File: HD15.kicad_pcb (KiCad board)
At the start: 2 copper layers, 110 x 62 mm, 46 parts, among them CN1 9, CN2 9, CN3 35RAPC4BH3, CN5 B6B-XH-A(LF)(SN), CN6 353180620, J1A JAMMA PINS 3.96MM PITCH 2.2MM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, J1B JAMMA PINS 3.96MM PITCH 2.2MM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, SW1 MJTP1230, SW2 MJTP1230, SW3 DIPSwitch-4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

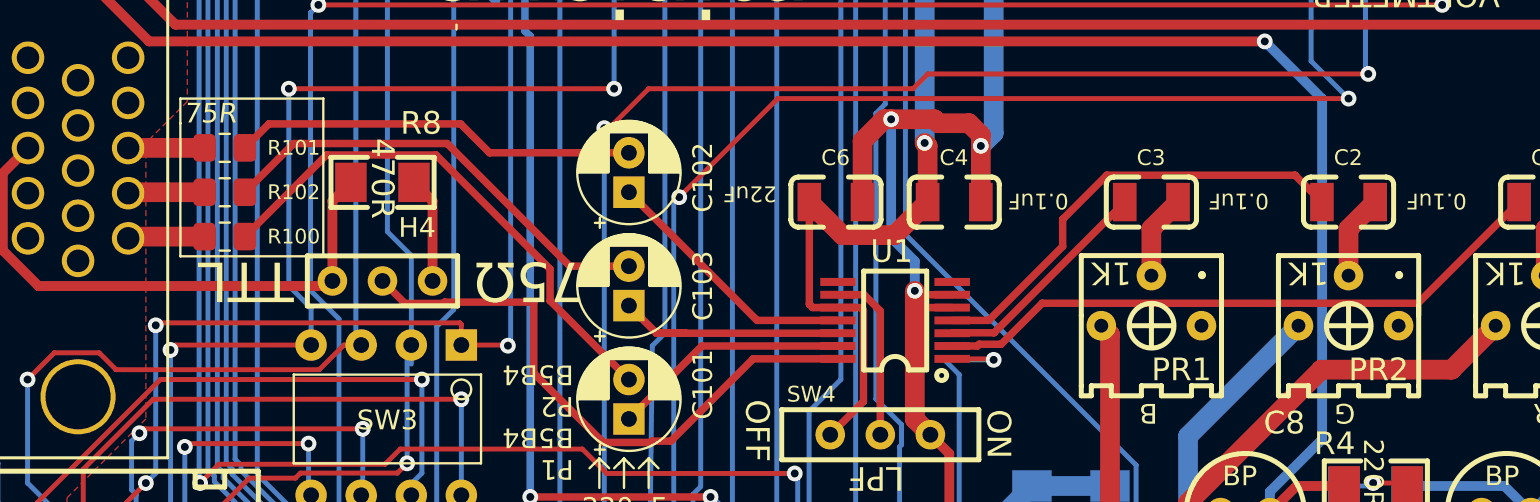
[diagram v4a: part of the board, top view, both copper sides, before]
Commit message: Fix RBG -> RGB screwup
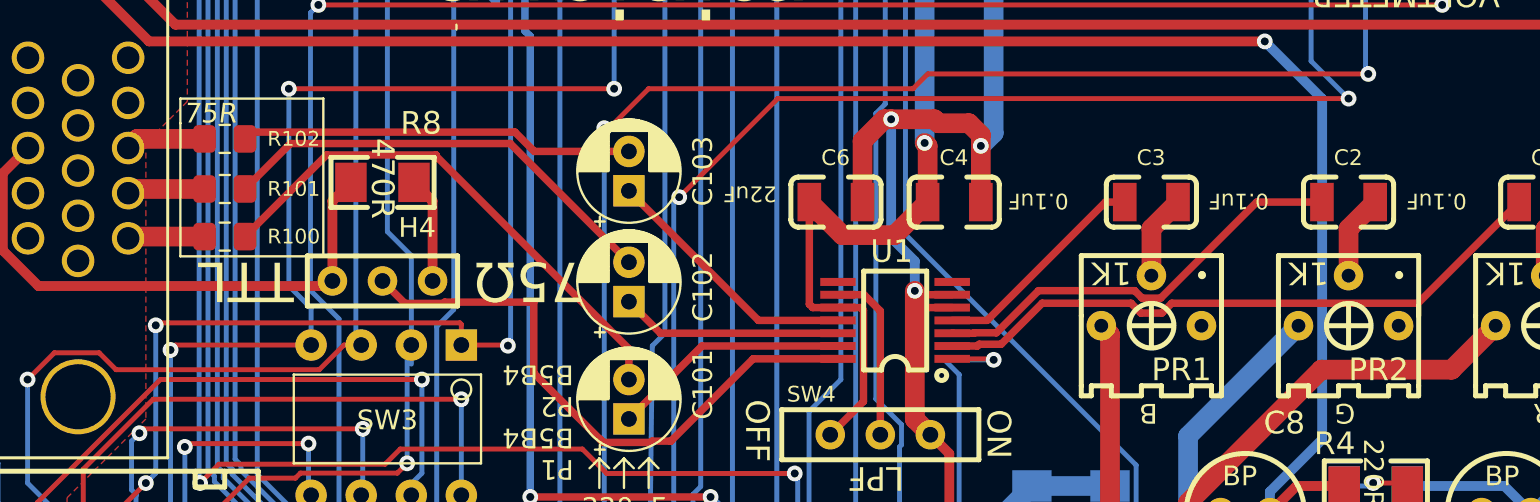
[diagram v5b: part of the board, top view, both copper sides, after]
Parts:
- moved C103 5.82 mm to (36.5, 13.4)
- moved C102 5.55 mm to (36.5, 19.1)
- moved R102 2.71 mm to (16.0, 10.8)
- moved R101 2.09 mm to (16.0, 13.3)
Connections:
- REF** pad 2: VIDEO_BLUE_5 -> VIDEO_GREEN_5
- REF** pad 3: VIDEO_GREEN_5 -> VIDEO_BLUE_5
- U1 pad 11: VIDEO_GREEN_3 -> VIDEO_BLUE_3
- U1 pad 12: VIDEO_BLUE_3 -> VIDEO_GREEN_3
- U1 pad 3: VIDEO_BLUE_2 -> VIDEO_GREEN_2
- U1 pad 4: VIDEO_GREEN_2 -> VIDEO_BLUE_2
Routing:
- net VIDEO_BLUE_3: track 20.5 -> 13.3 mm
- net VIDEO_BLUE_4: track 23.1 -> 20.0 mm
- net VIDEO_GREEN_4: track 20.6 -> 22.9 mm
- net VIDEO_GREEN_3: track 13.3 -> 11.3 mm
- net VIDEO_GREEN_2: track 23.2 -> 21.8 mm
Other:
- board text added: "HD15 mod by leadedsolder.com v3"
- board text removed: "HD15 mod by leadedsolder.com v2"
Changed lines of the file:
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@@
 			(layers "*.Cu" "*.Mask")
 			(remove_unused_layers no)
-			(net 69 "VIDEO_BLUE_5")
+			(net 68 "VIDEO_GREEN_5")
 		)
 		(pad "3" thru_hole circle
@@
 			(layers "*.Cu" "*.Mask")
 			(remove_unused_layers no)
-			(net 68 "VIDEO_GREEN_5")
+			(net 69 "VIDEO_BLUE_5")
 		)
 		(pad "4" thru_hole circle
@@
 	(footprint "Capacitor_THT:CP_Radial_D5.0mm_P2.00mm"
 		(layer "F.Cu")
-		(at 36.5 13.5 90)
+		(at 36.5 19.05 90)
 		(descr "CP, Radial series, Radial, pin pitch=2.00mm, , diameter=5mm, Electrolytic Capacitor")
 		(tags "CP Radial series Radial pin pitch 2.00mm  diameter 5mm Electrolytic Capacitor")
@@
 	(footprint "Resistor_SMD:R_0805_2012Metric_Pad1.15x1.40mm_HandSolder"
 		(layer "F.Cu")
-		(at 16 11.25)
+		(at 16 13.335)
 		(descr "Resistor SMD 0805 (2012 Metric), square (rectangular) end terminal, IPC_7351 nominal with elongated pad for handsoldering. (Body size source: https://docs.google.com/spreadsheets/d/1BsfQQcO9C6DZCsRaXUlFlo91Tg2WpOkGARC1WS5S8t0/edit?usp=sharing), generated with kicad-footprint-generator")
 		(tags "resistor handsolder")
@@
 	(footprint "Resistor_SMD:R_0805_2012Metric_Pad1.15x1.40mm_HandSolder"
 		(layer "F.Cu")
-		(at 16 13.5)
+		(at 16 10.795)
 		(descr "Resistor SMD 0805 (2012 Metric), square (rectangular) end terminal, IPC_7351 nominal with elongated pad for handsoldering. (Body size source: https://docs.google.com/spreadsheets/d/1BsfQQcO9C6DZCsRaXUlFlo91Tg2WpOkGARC1WS5S8t0/edit?usp=sharing), generated with kicad-footprint-generator")
 		(tags "resistor handsolder")
@@
 	(footprint "Capacitor_THT:CP_Radial_D5.0mm_P2.00mm"
 		(layer "F.Cu")
-		(at 36.5 19.25 90)
+		(at 36.5 13.43 90)
 		(descr "CP, Radial series, Radial, pin pitch=2.00mm, , diameter=5mm, Electrolytic Capacitor")
 		(tags "CP Radial series Radial pin pitch 2.00mm  diameter 5mm Electrolytic Capacitor")
@@
 			(size 1.803 0.406)
 			(layers "F.Cu" "F.Paste" "F.Mask")
-			(net 37 "VIDEO_BLUE_2")
+			(net 41 "VIDEO_GREEN_2")
 		)
 		(pad "4" smd rect
@@
 			(size 1.803 0.406)
 			(layers "F.Cu" "F.Paste" "F.Mask")
-			(net 41 "VIDEO_GREEN_2")
+			(net 37 "VIDEO_BLUE_2")
 		)
 		(pad "5" smd rect
@@
 			(size 1.803 0.406)
 			(layers "F.Cu" "F.Paste" "F.Mask")
-			(net 42 "VIDEO_GREEN_3")
+			(net 38 "VIDEO_BLUE_3")
 		)
 		(pad "12" smd rect
@@
 			(size 1.803 0.406)
 			(layers "F.Cu" "F.Paste" "F.Mask")
-			(net 38 "VIDEO_BLUE_3")
+			(net 42 "VIDEO_GREEN_3")
 		)
 		(pad "13" smd rect
@@
 	)
 	(gr_text "G"
-		(at 12.75 11.25 0)
+		(at 12.75 13.548192 0)
 		(layer "B.SilkS")
 		(effects
@@
 	)
 	(gr_text "B"
-		(at 12.75 13.5 0)
+		(at 12.7 11.258128 0)
 		(layer "B.SilkS")
 		(effects
@@
 		)
 	)
-	(gr_text "HD15 mod by leadedsolder.com v2"
+	(gr_text "HD15 mod by leadedsolder.com v3"
 		(at 108.204 32.512 0)
 		(layer "B.SilkS")
@@
 	)
 	(segment
-		(start 52.895 20.65)
-		(end 52.915013 20.629987)
+		(start 60.67 14)
+		(end 54.67 20)
 		(width 0.38)
 		(layer "F.Cu")
@@
 	)
 	(segment
-		(start 55.020013 20.629987)
-		(end 61.65 14)
+		(start 54.67 20)
+		(end 52.895 20)
 		(width 0.38)
 		(layer "F.Cu")
@@
 	)
 	(segment
-		(start 52.915013 20.629987)
-		(end 55.020013 20.629987)
+		(start 61.65 14)
+		(end 60.67 14)
 		(width 0.38)
 		(layer "F.Cu")
@@
 	)
 	(segment
-		(start 37.9 20.65)
-		(end 36.5 19.25)
-		(width 0.38)
-		(layer "F.Cu")
-		(net 38)
-	)
-	(segment
-		(start 39.4 20.65)
-		(end 39.286411 20.65)
-		(width 0.25)
-		(layer "F.Cu")
-		(net 38)
-	)
-	(segment
-		(start 47.104 20.65)
-		(end 37.9 20.65)
+		(start 47.104 20)
+		(end 43.07 20)
 		(width 0.38)
 		(layer "F.Cu")
@@
 	)
 	(segment
-		(start 39.4 20.65)
-		(end 37.9 20.65)
+		(start 43.07 20)
+		(end 36.5 13.43)
 		(width 0.38)
 		(layer "F.Cu")
@@
 	)
 	(segment
-		(start 47.104 20.65)
-		(end 39.4 20.65)
-		(width 0.25)
-		(layer "F.Cu")
-		(net 38)
-	)
-	(segment
 		(start 64.86 37)
 		(end 64.86 25.87)
@@
 	)
 	(segment
-		(start 70.284999 12.634999)
-		(end 60.737999 12.634999)
+		(start 52.895 20.65)
+		(end 54.006256 20.65)
 		(width 0.38)
 		(layer "F.Cu")
@@
 	)
 	(segment
-		(start 54.75 20)
-		(end 52.895 20)
+		(start 63.472204 18.87)
+		(end 68.342204 14)
+		(width 0.38)
+		(layer "F.Cu")
+		(net 41)
+	)
+	(segment
+		(start 68.342204 14)
+		(end 71.65 14)
+		(width 0.38)
+		(layer "F.Cu")
+		(net 41)
+	)
+	(segment
+		(start 52.895 20.65)
+		(end 52.915013 20.629987)
+		(width 0.38)
+		(layer "F.Cu")
+		(net 41)
+	)
+	(segment
+		(start 57.275354 18.493602)
+		(end 62.151398 18.493602)
 		(width 0.38)
 		(layer "F.Cu")
@@
 	)
 	(segment
-		(start 58.5 14.872998)
-		(end 58.5 16.25)
+		(start 62.527796 18.87)
+		(end 63.472204 18.87)
 		(width 0.38)
 		(layer "F.Cu")
@@
 	)
 	(segment
-		(start 58.5 16.25)
-		(end 54.75 20)
+		(start 54.006256 20.65)
+		(end 54.026258 20.629998)
 		(width 0.38)
 		(layer "F.Cu")
@@
 	)
 	(segment
-		(start 71.65 14)
-		(end 70.284999 12.634999)
+		(start 62.151398 18.493602)
+		(end 62.527796 18.87)
 		(width 0.38)
 		(layer "F.Cu")
@@
 	)
 	(segment
-		(start 60.737999 12.634999)
-		(end 58.5 14.872998)
+		(start 54.026258 20.629998)
+		(end 55.138958 20.629998)
 		(width 0.38)
 		(layer "F.Cu")
@@
 	)
 	(segment
-		(start 43 20)
-		(end 36.5 13.5)
+		(start 55.138958 20.629998)
+		(end 57.275354 18.493602)
+		(width 0.38)
+		(layer "F.Cu")
+		(net 41)
+	)
+	(segment
+		(start 38.1 20.65)
+		(end 36.5 19.05)
 		(width 0.38)
 		(layer "F.Cu")
@@
 	)
 	(segment
-		(start 47.104 20)
-		(end 43 20)
+		(start 47.104 20.65)
+		(end 38.1 20.65)
 		(width 0.38)
 		(layer "F.Cu")
@@
 	)
 	(segment
-		(start 55.379202 21.209998)
-		(end 54.266502 21.209998)
+		(start 81.65 14)
+		(end 76.520001 19.129999)
 		(width 0.38)
 		(layer "F.Cu")
@@
 	(segment
 		(start 76.520001 19.129999)
-		(end 57.459201 19.129999)
+		(end 64.032449 19.129999)
 		(width 0.38)
 		(layer "F.Cu")
@@
 	)
 	(segment
-		(start 81.65 14)
-		(end 76.520001 19.129999)
+		(start 63.532448 19.63)
+		(end 62.467552 19.63)
+		(width 0.38)
+		(layer "F.Cu")
+		(net 45)
+	)
+	(segment
+		(start 62.467552 19.63)
+		(end 61.967551 19.129999)
+		(width 0.38)
+		(layer "F.Cu")
+		(net 45)
+	)
+	(segment
+		(start 64.032449 19.129999)
+		(end 63.532448 19.63)
+		(width 0.38)
+		(layer "F.Cu")
+		(net 45)
+	)
+	(segment
+		(start 55.379202 21.209998)
+		(end 54.266502 21.209998)
 		(width 0.38)
 		(layer "F.Cu")
@@
 	)
 	(segment
+		(start 61.967551 19.129999)
+		(end 57.459201 19.129999)
+		(width 0.38)
+		(layer "F.Cu")
+		(net 45)
+	)
+	(segment
 		(start 54.266502 21.209998)
 		(end 54.1765 21.3)
@@
 	)
 	(segment
-		(start 26.712001 11.609999)
-		(end 32.5 17.397998)
+		(start 26.725 11.670244)
+		(end 36.5 21.445244)
 		(width 0.38)
 		(layer "F.Cu")
@@
 	)
 	(segment
-		(start 32.5 17.397998)
-		(end 32.5 19)
+		(start 17.025 15.75)
+		(end 21.165001 11.609999)
 		(width 0.38)
 		(layer "F.Cu")
@@
 	)
 	(segment
-		(start 32.5 19)
+		(start 36.5 21.445244)
 		(end 36.5 23)
 		(width 0.38)
@@
 	)
 	(segment
-		(start 21.165001 11.609999)
-		(end 17.025 15.75)
+		(start 26.712001 11.609999)
+		(end 26.725 11.622998)
 		(width 0.38)
 		(layer "F.Cu")
@@
 	)
 	(segment
-		(start 26.712001 11.609999)
-		(end 21.165001 11.609999)
+		(start 21.165001 11.609999)
+		(end 26.712001 11.609999)
 		(width 0.38)
 		(layer "F.Cu")
@@
 	)
 	(segment
-		(start 36.5 11.5)
-		(end 29.43002 11.5)
+		(start 26.725 11.622998)
+		(end 26.725 11.670244)
 		(width 0.38)
 		(layer "F.Cu")
-		(net 65)
+		(net 64)
 	)
 	(segment
-		(start 18.24001 10.03499)
-		(end 27.96501 10.03499)
+		(start 36.5 17.05)
+		(end 30.48 11.03)
 		(width 0.38)
 		(layer "F.Cu")
@@
 	)
 	(segment
-		(start 29.43002 11.5)
-		(end 27.96501 10.03499)
+		(start 19.33 11.03)
+		(end 17.025 13.335)
 		(width 0.38)
 		(layer "F.Cu")
@@
 	)
 	(segment
-		(start 17.025 11.25)
-		(end 18.24001 10.03499)
+		(start 30.48 11.03)
+		(end 19.33 11.03)
 		(width 0.38)
 		(layer "F.Cu")
@@
 	)
 	(segment
-		(start 36.5 17.25)
-		(end 33.5 17.25)
+		(start 36.5 11.43)
+		(end 31.700244 11.43)
 		(width 0.38)
 		(layer "F.Cu")
@@
 	)
 	(segment
-		(start 19.495012 11.029988)
-		(end 17.025 13.5)
+		(start 17.37 10.45)
+		(end 17.025 10.795)
 		(width 0.38)
 		(layer "F.Cu")
@@
 	)
 	(segment
-		(start 27.279988 11.029988)
-		(end 19.495012 11.029988)
+		(start 30.720244 10.45)
+		(end 17.37 10.45)
 		(width 0.38)
 		(layer "F.Cu")
@@
 	)
 	(segment
-		(start 33.5 17.25)
-		(end 27.279988 11.029988)
+		(start 31.700244 11.43)
+		(end 30.720244 10.45)
 		(width 0.38)
 		(layer "F.Cu")
@@
 	)
 	(segment
-		(start 11.109128 11.25)
-		(end 11.101 11.258128)
+		(start 11.314192 13.335)
+		(end 11.101 13.548192)
 		(width 1)
 		(layer "F.Cu")
@@
 	)
 	(segment
-		(start 14.975 11.25)
-		(end 11.109128 11.25)
+		(start 14.975 13.335)
+		(end 11.314192 13.335)
 		(width 1)
 		(layer "F.Cu")
@@
 	)
 	(segment
-		(start 14.975 13.5)
-		(end 11.149192 13.5)
+		(start 11.564128 10.795)
+		(end 11.101 11.258128)
 		(width 1)
 		(layer "F.Cu")
@@
 	)
 	(segment
-		(start 11.149192 13.5)
-		(end 11.101 13.548192)
+		(start 14.975 10.795)
+		(end 11.564128 10.795)
 		(width 1)
 		(layer "F.Cu")

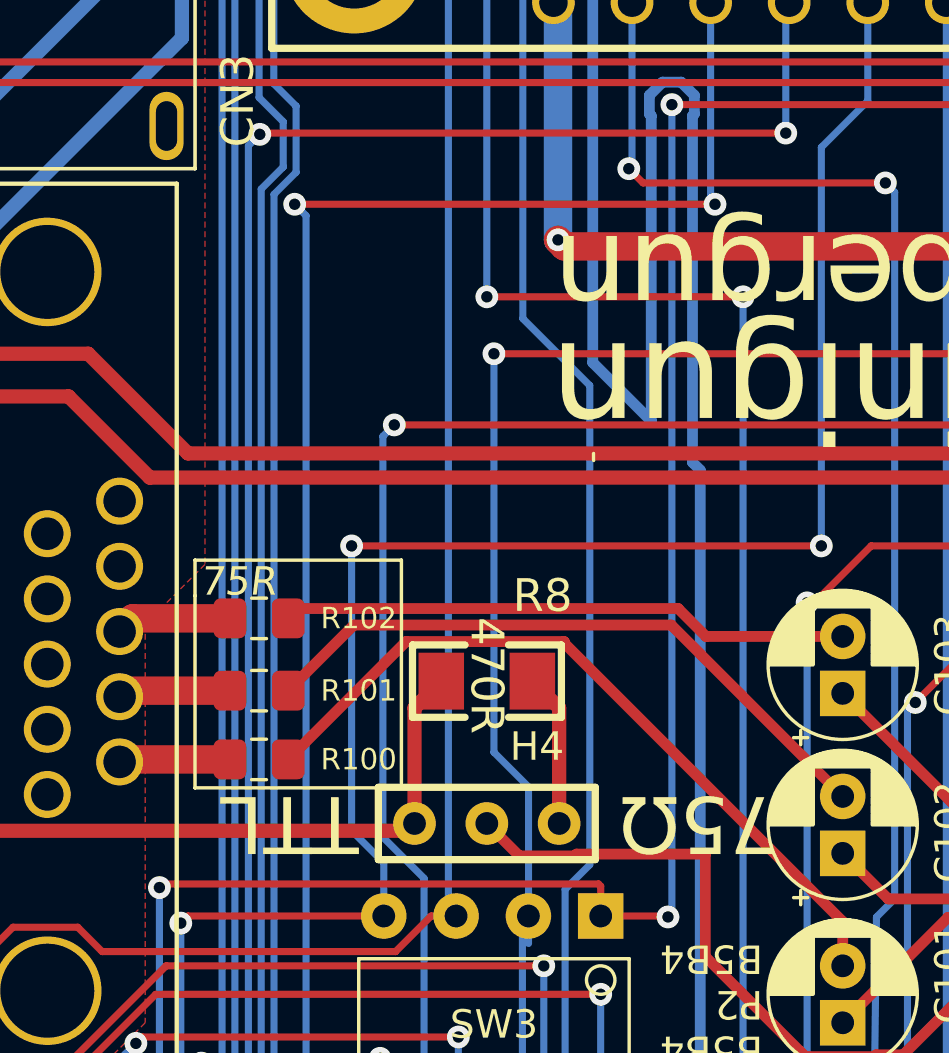
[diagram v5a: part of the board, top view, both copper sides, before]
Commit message: Make 75 ohm option obviously preferable
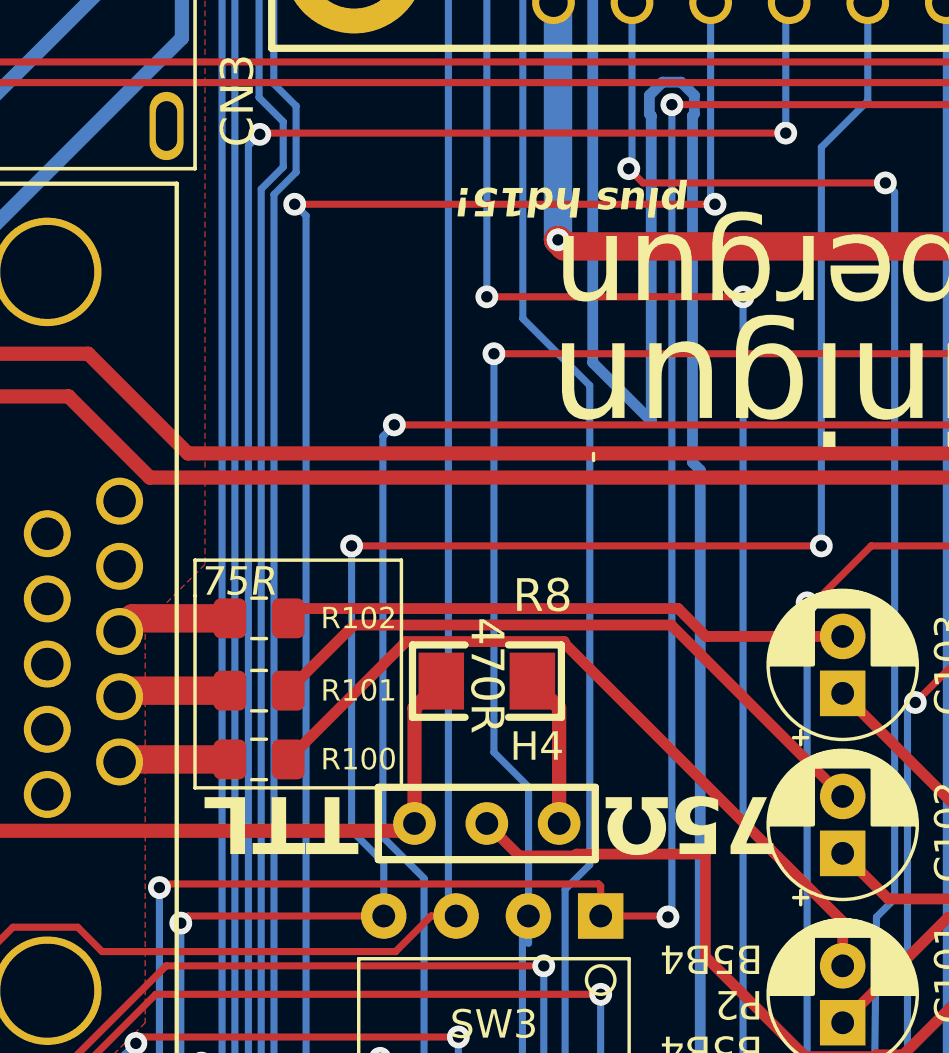
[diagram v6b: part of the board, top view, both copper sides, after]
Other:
- board text added: "HD15 mod by leadedsolder.com v2"
- board text added: "plus hd15!"
- board text removed: "HD15 mod by leadedsolder.com v3"
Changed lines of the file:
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@@
 		)
 	)
-	(gr_text "HD15 mod by leadedsolder.com v3"
+	(gr_text "HD15 mod by leadedsolder.com v2"
 		(at 108.204 32.512 0)
 		(layer "B.SilkS")
@@
 			(font
 				(size 2 2)
-				(thickness 0.06)
+				(thickness 0.4)
+				(bold yes)
 			)
 			(justify left)
@@
 			(font
 				(size 2 2)
-				(thickness 0.06)
+				(thickness 0.4)
+				(bold yes)
 			)
 			(justify left)
@@
 		)
 	)
+	(gr_text "plus hd15!"
+		(at 31.115 -4.445 180)
+		(layer "F.SilkS")
+		(effects
+			(font
+				(size 1 1)
+				(thickness 0.2)
+				(bold yes)
+				(italic yes)
+			)
+			(justify left bottom)
+		)
+	)
